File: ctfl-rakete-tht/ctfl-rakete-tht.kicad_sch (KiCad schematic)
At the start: 21 parts, among them J1 Conn_02x03_Odd_Even, SW1 SW_SPDT, U1 ATtiny212-SS

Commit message: finished layout for revision A
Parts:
- added JP1, JP2, JP3, JP4, JP5, JP6: SolderJumper_2_Open, Jumper:SolderJumper-2_P1.3mm_Open_RoundedPad1.0x1.5mm, symbol Jumper:SolderJumper_2_Open
- SW1: footprint Button_Switch_SMD:SW_SPDT_CK_JS102011SAQN -> local:SW_SPDT_ESP4020
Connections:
- net +3V0: now also JP1.2 (B), JP2.2 (B), JP3.2 (B), JP4.2 (B), JP5.2 (B), JP6.2 (B)
- net flame_inner: now also U1.7 (PA3), JP5.1 (A); no longer U1.2 (PA6)
- net flame_outer: now also U1.5 (PA2), JP6.1 (A); no longer U1.3 (PA7)
- net light_center: now also U1.3 (PA7), JP3.1 (A); no longer U1.5 (PA2)
- net light_left: now also U1.2 (PA6), JP2.1 (A); no longer U1.4 (PA1)
- net light_right: now also U1.4 (PA1), JP4.1 (A); no longer U1.7 (PA3)
- net at BT1.1 (+), SW1.3 (C): now also JP1.1 (A)
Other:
- moved on the sheet: SW1

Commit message: replaced in-flame LED footprints with 0805-only version and reoriented them
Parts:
- D12, D13, D14, D6, D7, D8, D9: footprint local:LED_combo_0805_5mmSMD_HandSolder -> local:LED_0805_SMD_HandSolder
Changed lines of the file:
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@@
 			)
 		)
-		(property "Footprint" "local:LED_combo_0805_5mmSMD_HandSolder"
+		(property "Footprint" "local:LED_0805_SMD_HandSolder"
 			(at 246.38 133.35 90)
 			(effects
@@
 			)
 		)
-		(property "Footprint" "local:LED_combo_0805_5mmSMD_HandSolder"
+		(property "Footprint" "local:LED_0805_SMD_HandSolder"
 			(at 195.58 133.35 90)
 			(effects
@@
 			)
 		)
-		(property "Footprint" "local:LED_combo_0805_5mmSMD_HandSolder"
+		(property "Footprint" "local:LED_0805_SMD_HandSolder"
 			(at 256.54 133.35 90)
 			(effects
@@
 			)
 		)
-		(property "Footprint" "local:LED_combo_0805_5mmSMD_HandSolder"
+		(property "Footprint" "local:LED_0805_SMD_HandSolder"
 			(at 185.42 133.35 90)
 			(effects
@@
 			)
 		)
-		(property "Footprint" "local:LED_combo_0805_5mmSMD_HandSolder"
+		(property "Footprint" "local:LED_0805_SMD_HandSolder"
 			(at 266.7 133.35 90)
 			(effects
@@
 			)
 		)
-		(property "Footprint" "local:LED_combo_0805_5mmSMD_HandSolder"
+		(property "Footprint" "local:LED_0805_SMD_HandSolder"
 			(at 205.74 133.35 90)
 			(effects
@@
 			)
 		)
-		(property "Footprint" "local:LED_combo_0805_5mmSMD_HandSolder"
+		(property "Footprint" "local:LED_0805_SMD_HandSolder"
 			(at 215.9 133.35 90)
 			(effects

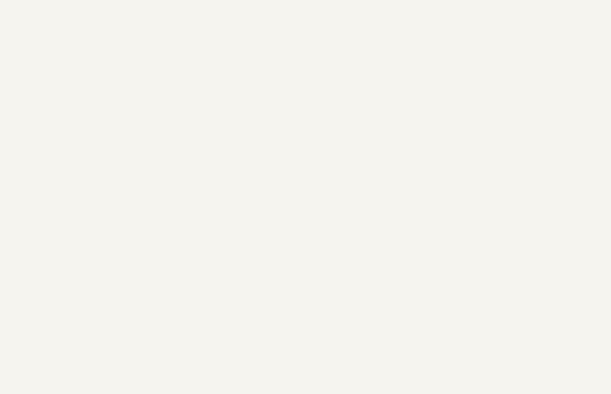
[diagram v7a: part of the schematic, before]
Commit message: added hanging wire solder points and updated renders
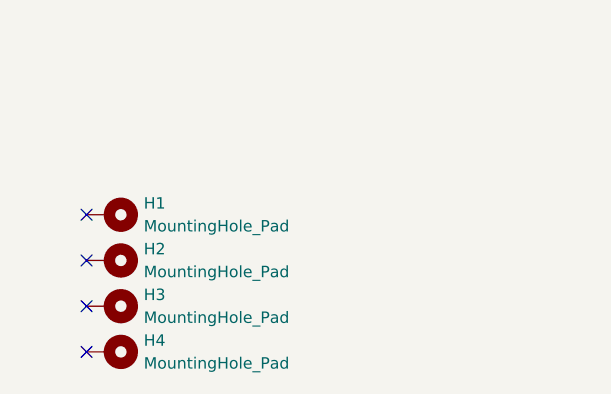
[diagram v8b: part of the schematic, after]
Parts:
- added H1, H2, H3, H4: MountingHole_Pad, local:wire_pad, symbol Mechanical:MountingHole_Pad
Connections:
- no-connect marks 4 -> 8
